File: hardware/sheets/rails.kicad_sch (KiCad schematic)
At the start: 55 parts, among them U1 LM5164DDA, U2 LM5164DDA, U3 LM51571-Q1, U4 DML3017LDC

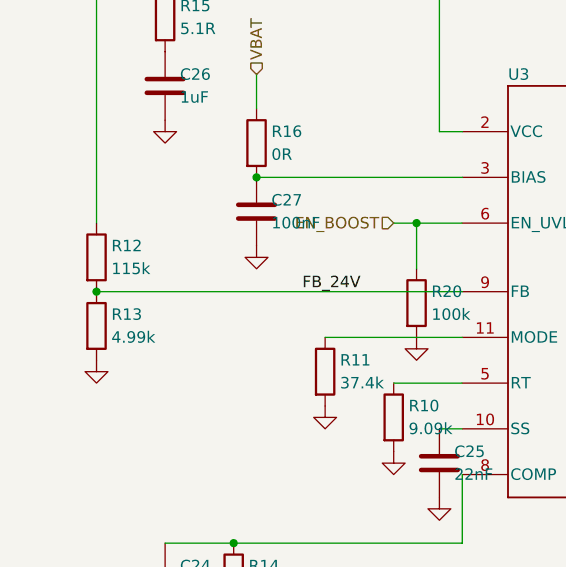
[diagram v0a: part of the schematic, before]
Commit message: hw(sch): Task 7 schematic review - three defects found and fixed
Every spec requirement traced to a sheet and refdes, read back from the
exported netlist rather than the drawing. 29 of 31 rows PASS; two carried
forward. Full write-up in hardware/docs/schematic-review.md.

F1 - Q1 carried the superseded SQJ415EP. That part was replaced by the
SQJ461EP on 2026-09-13 precisely because it is a 40 V device and the
SMBJ24A clamps at 38.9 V - 2.8% margin on the one part that sees every
vehicle transient. The replacement reached part-selection.md and the spec
but never the schematic, so a BOM built from it would have ordered the
wrong FET. Also closes the open gate-drive question: D1/R1 put Vgs at
-11 to -12.6 V, so the 16 mOhm column applies and the 0.78 W figure stands.

F2 - R2 and R3, the 0R links that short both windings of the common-mode
choke L2, were not marked DNP. A BOM would have stuffed the choke AND the
links; the links win and L2 becomes decorative. The board would work
perfectly and filter nothing, with no ERC or DRC check saying a word.
Both are now DNP, and gen_power_input.py learned to emit (dnp yes).

F3 - the 24 V feedback divider (115k/4.99k = 120k) conducts in deep sleep:
with the boost disabled, +24V still sits at ~12.35 V through L3 and D4, so
the divider drew 103 uA - larger than every other sleep contributor
combined, and absent from the spec 8.2 budget. Raised to 576k/24.9k, same
ratio, 20.5 uA. Revised budget ~94 uA typ / ~111 uA max against the 200 uA
target. C61 (10 pF, DNP) fitted as a Cff stuff option for the higher FB
impedance.

Carried forward: F4 (L1/L2 carry the full 7.0 A and have no thermal budget
- a 22 mOhm total DCR ceiling is now specified) and F5 (the spec's second
feed DNP footprints do not exist; needs a decision before Task 8 commits
to an outline).

Verification: ERC --severity-all --exit-code-violations exit=0, 0 errors,
0 warnings. 166 nets, unchanged by the fixes. DNP set read back from the
sheets: 31 parts. All six genera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
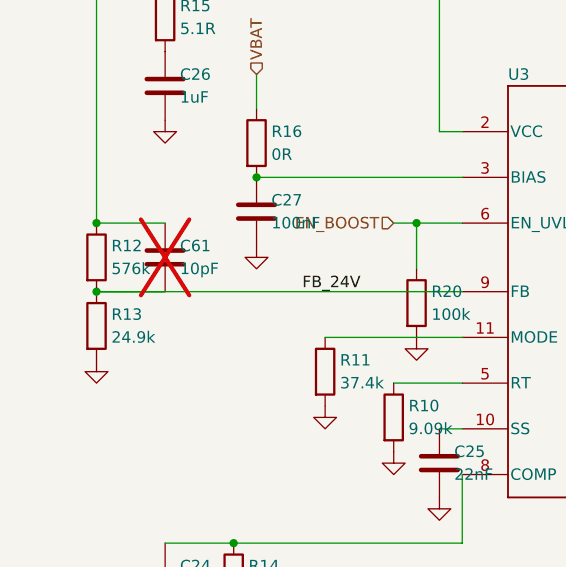
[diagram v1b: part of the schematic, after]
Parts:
- added C61: 10pF, symbol Device:C
- R12: value 115k -> 576k
- R13: value 4.99k -> 24.9k
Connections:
- net +24V: now also C61.1
- net FB_24V: now also C61.2
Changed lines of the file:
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@@
 	)
 	(junction
+		(at 30.48 134.62)
+		(diameter 0)
+		(color 0 0 0 0)
+	)
+	(junction
 		(at 76.2 45.72)
 		(diameter 0)
@@
 	(wire
 		(pts
+			(xy 38.1 142.24) (xy 30.48 142.24)
+		)
+		(stroke
+			(width 0)
+			(type default)
+		)
+	)
+	(wire
+		(pts
 			(xy 71.12 147.32) (xy 55.88 147.32)
 		)
@@
 	(wire
 		(pts
+			(xy 30.48 134.62) (xy 38.1 134.62)
+		)
+		(stroke
+			(width 0)
+			(type default)
+		)
+	)
+	(wire
+		(pts
 			(xy 116.84 195.58) (xy 116.84 190.5)
 		)
@@
 	)
 	(symbol
+		(lib_id "Device:C")
+		(at 38.1 138.43 0)
+		(unit 1)
+		(body_style 1)
+		(exclude_from_sim no)
+		(in_bom yes)
+		(on_board yes)
+		(in_pos_files yes)
+		(dnp yes)
+		(property "Reference" "C61"
+			(at 39.751 137.16 0)
+			(show_name no)
+			(do_not_autoplace no)
+			(effects
+				(font
+					(size 1.27 1.27)
+				)
+				(justify left)
+			)
+		)
+		(property "Value" "10pF"
+			(at 39.751 139.7 0)
+			(show_name no)
+			(do_not_autoplace no)
+			(effects
+				(font
+					(size 1.27 1.27)
+				)
+				(justify left)
+			)
+		)
+		(property "Footprint" ""
+			(at 38.1 138.43 0)
+			(hide yes)
+			(show_name no)
+			(do_not_autoplace no)
+			(effects
+				(font
+					(size 1.27 1.27)
+				)
+			)
+		)
+		(property "Datasheet" ""
+			(at 38.1 138.43 0)
+			(hide yes)
+			(show_name no)
+			(do_not_autoplace no)
+			(effects
+				(font
+					(size 1.27 1.27)
+				)
+			)
+		)
+		(property "Description" ""
+			(at 38.1 138.43 0)
+			(hide yes)
+			(show_name no)
+			(do_not_autoplace no)
+			(effects
+				(font
+					(size 1.27 1.27)
+				)
+			)
+		)
+		(pin "1"
+		)
+		(pin "2"
+		)
+		(instances
+			(project "mccan"
+				(path "/7410bb74-5653-4f1b-8c7c-ce17eb633f20/4a66277e-62b8-454b-8781-170494cf9f57"
+					(reference "C61")
+					(unit 1)
+				)
+			)
+		)
+	)
+	(symbol
 		(lib_id "Device:R")
 		(at 101.6 199.39 0)
@@
 			)
 		)
-		(property "Value" "4.99k"
+		(property "Value" "24.9k"
 			(at 32.131 147.32 0)
 			(show_name no)
@@
 			)
 		)
-		(property "Value" "115k"
+		(property "Value" "576k"
 			(at 32.131 139.7 0)
 			(show_name no)

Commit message: hw(sch): sweep every selected part into the schematic; D6+D7 become one PESD2CANFD24U-T
Closes the gap the Task 7 review's finding F1 was about: parts chosen in
prose had not reached the generators, which is exactly how the superseded
SQJ415EP survived five days in the schematic.

STRUCTURAL - the CAN ESD pair is now one part. D6 and D7 were two placeholder
"24V bidir" discretes; the Nexperia PESD2CANFD24U-T is a single SOT23 holding
both bidirectional elements (K1/K2/CC). New verified symbol in symlib.py built
from Table 2 of the datasheet, added to gen_mcu_can's lib_symbols, and
Device:D_TVS dropped from that sheet since D6/D7 were its only users.

The two protected pins land exactly on the CANH and CANL runs, so each run is
drawn as TWO segments meeting AT the pin rather than one segment the pin
happens to touch. A pin sitting mid-wire does connect, but this project has
already produced one silent connectivity defect of that shape (labels
mid-wire, 14 instances), so the pin is made a wire endpoint and junctioned.
Verified from the netlist rather than from ERC: D6.1 -> /CANH, D6.2 -> /CANL,
D6.3 -> GND.

Consolidating freed D7, so the diode series was renumbered to stay gapless:
the ignition-divider BAT54 D8 -> D7, the twelve RGB sense clamps D9-D20 ->
D8-D19, and the PROFET sense clamp D21 -> D20. Every designator series is
gapless: C1-61, D1-20, F1-5, J1-8, L1-6, Q1-9, R1-99, SW1-2, U1-9.

VALUE SWEEP - L4/L5 "22uH" -> XAL7070-223ME, L6 "51uH CM choke" ->
ACT45B-510-2P-TL003, C3 "220uF" -> "220uF 63V" (the SMBJ24A's 8/20 us clamp is
50.6 V, so a 50 V part has no margin), U7 -> PCA9685PW/Q900, the only
AEC-Q100 variant in the ordering table. U7's lib_id stays Driver_LED:PCA9685PW
- that is the stock symbol's name, and the package is the same TSSOP28. D4 was
already SS5PH102.

FOOTPRINT - installed the vendor SamacSys footprint and STEP model for the
Wurth choke as footprints/mccan.pretty/Wurth_WE-CMBNC_7448031002.kicad_mod and
3dmodels/. Its pads verify against t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
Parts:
- L4, L5: value 22uH -> XAL7070-223ME
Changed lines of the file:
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@@
 			)
 		)
-		(property "Value" "22uH"
+		(property "Value" "XAL7070-223ME"
 			(at 111.76 80.01 90)
 			(show_name no)
@@
 			)
 		)
-		(property "Value" "22uH"
+		(property "Value" "XAL7070-223ME"
 			(at 111.76 34.29 90)
 			(show_name no)

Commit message: hw(pcb): Task 8 step 0 - footprints assigned, 209 of 219 verified
Nothing in the project had a footprint except the PROFET's. Assignment now
lives in one auditable place, scripts/fpmap.py, which the four sheet
generators call when emitting each symbol's Footprint property. No generator
chooses a footprint of its own any more.

Three rules, and the reasoning is in the file rather than in a commit nobody
will read again: signal passives are 0603; a passive gets a bigger package
only for a stated reason; and nothing gets a footprint that has not been
checked to exist.

The reasons that drove a larger package:
- R2/R3, the 0R links bypassing the input choke windings, are 2512. They are
  DNP, but if anyone fits them for the tied-ground prototype they carry the
  entire 7.0 A night load, and a 0603 link is rated about 1 A.
- R52-R63, the RGB sense shunts, are 1206 for the FAULT case, not the normal
  7 mW. The package is sized on the understanding that firmware latches a
  shorted channel off; if that is ever dropped they must become 2512 1 W.
- The front-end ceramics are sized against the SMBJ24A's 8/20 us clamp of
  50.6 V, not the 38.9 V the distributor summaries quote. 100 nF fits 0805 at
  100 V; 1-2.2 uF at 63 V does not fit 0805; 10 uF at 63 V needs 1210.
- C20-C22 on +24 V are 1206 for DC-BIAS derating, a different reason - a 25 V
  X7R at 24 V keeps only 40-60% of nameplate.

Package identifications read from the datasheets rather than assumed:
NX5020UNBKS is SOT363/SC-88 (section 1), LM51571-Q1 RTE is WQFN-16 3x3 with a
1.66 mm exposed pad (so KiCad's EP1.675x1.675 is within tolerance), SS5PH102
is TO-277A, PESD2CANFD24U-T is SOT23.

FLAGGED, not silently accepted: the LM5164 DDA thermal pad is 3.4 x 2.8 mm on
the mechanical drawing and KiCad has no exact match. EP2.62x3.51 is the
closest by area (9.20 mm2 against 9.52) and is used for now, but that pad is
the part's heatsink on a thermally critical rail, so an exact DDA land pattern
should be drawn before fabr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
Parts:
- C10, C11, C14, C15, C16, C17, C23, C24, C25, C26, C27, C28, C29, C30, C31, C32, C33, C34, C61, C8, C9: footprint (none) -> Capacitor_SMD:C_0603_1608Metric
- C12, C20, C21, C22, C6: footprint (none) -> Capacitor_SMD:C_1206_3216Metric
- C13, C7: footprint (none) -> Capacitor_SMD:C_0805_2012Metric
- C18, C19: footprint (none) -> Capacitor_SMD:C_1210_3225Metric
- D4: footprint (none) -> Package_TO_SOT_SMD:TO-277A
- L3: footprint (none) -> Inductor_SMD:L_Coilcraft_XAL4030-XXX
- L4, L5: footprint (none) -> Inductor_SMD:L_Coilcraft_XAL7070-XXX
- R10, R11, R12, R13, R14, R15, R16, R17, R18, R19, R20, R21, R4, R5, R6, R7, R8, R9: footprint (none) -> Resistor_SMD:R_0603_1608Metric
- U1, U2: footprint (none) -> Package_SO:SOIC-8-1EP_3.9x4.9mm_P1.27mm_EP2.62x3.51mm
- U3: footprint (none) -> Package_DFN_QFN:QFN-16-1EP_3x3mm_P0.5mm_EP1.675x1.675mm
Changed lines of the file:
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@@
 			)
 		)
-		(property "Footprint" ""
+		(property "Footprint" "Capacitor_SMD:C_1206_3216Metric"
 			(at 48.26 67.31 0)
 			(hide yes)
@@
 			)
 		)
-		(property "Footprint" ""
+		(property "Footprint" "Capacitor_SMD:C_0603_1608Metric"
 			(at 38.1 138.43 0)
 			(hide yes)
@@
 			)
 		)
-		(property "Footprint" ""
+		(property "Footprint" "Resistor_SMD:R_0603_1608Metric"
 			(at 101.6 199.39 0)
 			(hide yes)
@@
 			)
 		)
-		(property "Footprint" ""
+		(property "Footprint" "Resistor_SMD:R_0603_1608Metric"
 			(at 38.1 111.76 0)
 			(hide yes)
@@
 			)
 		)
-		(property "Footprint" ""
+		(property "Footprint" "Resistor_SMD:R_0603_1608Metric"
 			(at 55.88 151.13 0)
 			(hide yes)
@@
 			)
 		)
-		(property "Footprint" ""
+		(property "Footprint" "Capacitor_SMD:C_1210_3225Metric"
 			(at 134.62 118.11 0)
 			(hide yes)
@@
 			)
 		)
-		(property "Footprint" ""
+		(property "Footprint" "Capacitor_SMD:C_1206_3216Metric"
 			(at 157.48 130.81 0)
 			(hide yes)
@@
 			)
 		)
-		(property "Footprint" ""
+		(property "Footprint" "Resistor_SMD:R_0603_1608Metric"
 			(at 30.48 146.05 0)
 			(hide yes)
@@
 			)
 		)
-		(property "Footprint" ""
+		(property "Footprint" "Capacitor_SMD:C_0603_1608Metric"
 			(at 96.52 72.39 0)
 			(hide yes)
@@
 			)
 		)
-		(property "Footprint" ""
+		(property "Footprint" "Capacitor_SMD:C_0603_1608Metric"
 			(at 68.58 161.29 0)
 			(hide yes)
@@
 			)
 		)
-		(property "Footprint" ""
+		(property "Footprint" "Capacitor_SMD:C_1206_3216Metric"
 			(at 149.86 130.81 0)
 			(hide yes)
@@
 			)
 		)
-		(property "Footprint" ""
+		(property "Footprint" "Capacitor_SMD:C_0805_2012Metric"
 			(at 40.64 67.31 0)
 			(hide yes)
@@
 			)
 		)
-		(property "Footprint" ""
+		(property "Footprint" "Resistor_SMD:R_0603_1608Metric"
 			(at 45.72 173.99 0)
 			(hide yes)
@@
 			)
 		)
-		(property "Footprint" ""
+		(property "Footprint" "Resistor_SMD:R_0603_1608Metric"
 			(at 63.5 156.21 0)
 			(hide yes)
@@
 			)
 		)
-		(property "Footprint" ""
+		(property "Footprint" "Resistor_SMD:R_0603_1608Metric"
 			(at 50.8 199.39 0)
 			(hide yes)
@@
 			)
 		)
-		(property "Footprint" ""
+		(property "Footprint" "Resistor_SMD:R_0603_1608Metric"
 			(at 58.42 41.91 0)
 			(hide yes)
@@
 			)
 		)
-		(property "Footprint" ""
+		(property "Footprint" "Capacitor_SMD:C_0603_1608Metric"
 			(at 132.08 34.29 0)
 			(hide yes)
@@
 			)
 		)
-		(property "Footprint" ""
+		(property "Footprint" "Capacitor_SMD:C_1210_3225Metric"
 			(at 142.24 118.11 0)
 			(hide yes)
@@
 			)
 		)
-		(property "Footprint" ""
+		(property "Footprint" "Resistor_SMD:R_0603_1608Metric"
 			(at 116.84 87.63 0)
 			(hide yes)
@@
 			)
 		)
-		(property "Footprint" ""
+		(property "Footprint" "Resistor_SMD:R_0603_1608Metric"
 			(at 248.92 46.99 0)
 			(hide yes)
@@
 			)
 		)
-		(property "Footprint" ""
+		(property "Footprint" "Capacitor_SMD:C_0805_2012Metric"
 			(at 50.8 29.21 0)
 			(hide yes)
@@
 			)
 		)
-		(property "Footprint" ""
+		(property "Footprint" "Resistor_SMD:R_0603_1608Metric"
 			(at 53.34 85.09 0)
 			(hide yes)
@@
 			)
 		)
-		(property "Footprint" ""
+		(property "Footprint" "Capacitor_SMD:C_0603_1608Metric"
 			(at 66.04 199.39 0)
 			(hide yes)
@@
 			)
 		)
-		(property "Footprint" ""
+		(property "Footprint" "Capacitor_SMD:C_0603_1608Metric"
 			(at 38.1 119.38 0)
 			(hide yes)
@@
 			)
 		)
-		(property "Footprint" ""
+		(property "Footprint" "Capacitor_SMD:C_0603_1608Metric"
 			(at 139.7 34.29 0)
 			(hide yes)
@@
 			)
 		)
-		(property "Footprint" ""
+		(property "Footprint" "Capacitor_SMD:C_1206_3216Metric"
 			(at 142.24 130.81 0)
 			(hide yes)
@@
 			)
 		)
-		(property "Footprint" ""
+		(property "Footprint" "Capacitor_SMD:C_0603_1608Metric"
 			(at 38.1 173.99 0)
 			(hide yes)
@@
 			)
 		)
-		(property "Footprint" ""
+		(property "Footprint" "Inductor_SMD:L_Coilcraft_XAL7070-XXX"
 			(at 107.95 76.2 0)
 			(hide yes)
@@
 			)
 		)
-		(property "Footprint" ""
+		(property "Footprint" "Package_SO:SOIC-8-1EP_3.9x4.9mm_P1.27mm_EP2.62x3.51mm"
 			(at 76.2 78.74 0)
 			(hide yes)
@@
 			)
 		)
-		(property "Footprint" ""
+		(property "Footprint" "Capacitor_SMD:C_0603_1608Metric"
 			(at 264.16 39.37 0)
 			(hide yes)
@@
 			)
 		)
-		(property "Footprint" ""
+		(property "Footprint" "Capacitor_SMD:C_0603_1608Metric"
 			(at 205.74 39.37 0)
 			(hide yes)
@@
 			)
 		)
-		(property "Footprint" ""
+		(property "Footprint" "Capacitor_SMD:C_0603_1608Metric"
 			(at 96.52 26.67 0)
 			(hide yes)
@@
 			)
 		)
-		(property "Footprint" ""
+		(property "Footprint" "Capacitor_SMD:C_0603_1608Metric"
 			(at 215.9 57.15 0)
 			(hide yes)
@@
 			)
 		)
-		(property "Footprint" ""
+		(property "Footprint" "Capacitor_SMD:C_0603_1608Metric"
 			(at 198.12 39.37 0)
 			(hide yes)
@@
 			)
 		)
-		(property "Footprint" ""
+		(property "Footprint" "Resistor_SMD:R_0603_1608Metric"
 			(at 116.84 41.91 0)
 			(hide yes)
@@
 			)
 		)
-		(property "Footprint" ""
+		(property "Footprint" "Capacitor_SMD:C_1206_3216Metric"
 			(at 43.18 29.21 0)
 			(hide yes)
@@
 			)
 		)
-		(property "Footprint" ""
+		(property "Footprint" "Resistor_SMD:R_0603_1608Metric"
 			(at 58.42 87.63 0)
 			(hide yes)
@@
 			)
 		)
-		(property "Footprint" ""
+		(property "Footprint" "Capacitor_SMD:C_0603_1608Metric"
 			(at 132.08 80.01 0)
 			(hide yes)
@@
 			)
 		)
-		(property "Footprint" ""
+		(property "Footprint" "Capacitor_SMD:C_0603_1608Metric"
 			(at 45.72 181.61 0)
 			(hide yes)
@@
 			)
 		)
-		(property "Footprint" ""
+		(property "Footprint" "Resistor_SMD:R_0603_1608Metric"
 			(at 48.26 125.73 0)
 			(hide yes)
@@
 			)
 		)
-		(property "Footprint" ""
+		(property "Footprint" "Capacitor_SMD:C_0603_1608Metric"
 			(at 50.8 207.01 0)
 			(hide yes)
@@
 			)
 		)
-		(property "Footprint" ""
+		(property "Footprint" "Resistor_SMD:R_0603_1608Metric"
 			(at 66.04 143.51 0)
 			(hide yes)
@@
 			)
 		)
-		(property "Footprint" ""
+		(property "Footprint" "Inductor_SMD:L_Coilcraft_XAL7070-XXX"
 			(at 107.95 30.48 0)
 			(hide yes)
@@
 			)
 		)
-		(property "Footprint" ""
+		(property "Footprint" "Capacitor_SMD:C_0603_1608Metric"
 			(at 256.54 39.37 0)
 			(hide yes)
@@
 			)
 		)
-		(property "Footprint" ""
+		(property "Footprint" "Capacitor_SMD:C_0603_1608Metric"
 			(at 101.6 207.01 0)
 			(hide yes)
@@
 			)
 		)
-		(property "Footprint" ""
+		(property "Footprint" "Package_DFN_QFN:QFN-16-1EP_3x3mm_P0.5mm_EP1.675x1.675mm"
 			(at 96.52 142.24 0)
 			(hide yes)
@@
 			)
 		)
-		(property "Footprint" ""
+		(property "Footprint" "Package_SO:SOIC-8-1EP_3.9x4.9mm_P1.27mm_EP2.62x3.51mm"
 			(at 76.2 33.02 0)
 			(hide yes)
@@
 			)
 		)
-		(property "Footprint" ""
+		(property "Footprint" "Resistor_SMD:R_0603_1608Metric"
 			(at 116.84 34.29 0)
 			(hide yes)
@@
 			)
 		)
-		(property "Footprint" ""
+		(property "Footprint" "Inductor_SMD:L_Coilcraft_XAL4030-XXX"
 			(at 127 118.11 0)
 			(hide yes)
@@
 			)
 		)
-		(property "Footprint" ""
+		(property "Footprint" "Resistor_SMD:R_0603_1608Metric"
 			(at 116.84 80.01 0)
 			(hide yes)
@@
 			)
 		)
-		(property "Footprint" ""
+		(property "Footprint" "Capacitor_SMD:C_0603_1608Metric"
 			(at 139.7 80.01 0)
 			(hide yes)
@@
 			)
 		)
-		(property "Footprint" ""
+		(property "Footprint" "Resistor_SMD:R_0603_1608Metric"
 			(at 30.48 138.43 0)
 			(hide yes)
@@
 			)
 		)
-		(property "Footprint" ""
+		(property "Footprint" "Capacitor_SMD:C_0603_1608Metric"
 			(at 48.26 133.35 0)
 			(hide yes)
@@
 			)
 		)
-		(property "Footprint" ""
+		(property "Footprint" "Capacitor_SMD:C_0603_1608Metric"
 			(at 116.84 199.39 0)
 			(hide yes)
@@
 			)
 		)
-		(property "Footprint" ""
+		(property "Footprint" "Package_TO_SOT_SMD:TO-277A"
 			(at 134.62 127 0)
 			(hide yes)

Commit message: hw(pcb): resolve D4 and U4, give GND_IN its own island, stop leaving stubs
Four things that had all been blocking a clean board, plus the pass of routing
they unblocked.

D4 is a TO-277A, whose third pad is the cathode tab.  Device:D_Schottky has no
pin 3, so schematic parity reported the tab as a net with no corresponding pin
however the pad was aliased -- aliasing pads is not a fix for a symbol that is
missing a pin.  mccan_parts:D_SCHOTTKY_TAB is that symbol with a hidden pin 3
stacked on the cathode, which is what the part actually is.

U4 was BLOCKED since Task 8 step 0 on an apparent pin-1 disagreement between two
figures of DS46371.  There is no disagreement: the Suggested Pad Layout is a bare
land pattern with no pin names, drawn in a different orientation from the Package
Outline, and the three figures that do carry pin names all agree.  Pin 1 top-left
in top view, counter-clockwise; pad 13 is the exposed pad and it is VIN, not GND.
The reasoning is written out in fpmap.py so it is not re-litigated.  fpmap's
unassignable list is now empty and says why it should stay that way.

GND_IN gets its own F.Cu island rather than sharing the pour.  GND and GND_IN are
separate nets that meet at exactly two places, L2 winding B and R3; nothing in DRC
enforces that, because a pour never shorts to a foreign net, so check_grounds.py
is the guard and it now passes: all 12 GND_IN pads inside the island, no GND pads
in it.

_ar_prune was deleting whole tracks when it should have been trimming them, and
was doing its reachability walk without regard for which layer a piece was on.
It is now layer-aware and junction-based, and trims rather than deletes.  That
takes the board from 9 dangling vias and 1 dangling track to none of either.

Also: SolderWire footprints are BOM-excluded in the library and the symbols
disagreed, which parity reported seven times over -- the footprints are right, so
in_bom() now follows them.  Silk references that collided move to F.Fab instead
of bein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
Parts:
- D4: symbol Device:D_Schottky -> mccan_parts:D_SCHOTTKY_TAB
- U4: footprint (none) -> Package_DFN_QFN:DFN-12-1EP_3x3mm_P0.5mm_EP2.05x2.86mm
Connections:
- net +24V: now also D4.3 (K)
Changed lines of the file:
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@@
 			)
 		)
-		(property "Footprint" ""
+		(property "Footprint" "Package_DFN_QFN:DFN-12-1EP_3x3mm_P0.5mm_EP2.05x2.86mm"
 			(at 228.6 45.72 0)
 			(hide yes)
@@
 	)
 	(symbol
-		(lib_id "Device:D_Schottky")
+		(lib_id "mccan_parts:D_SCHOTTKY_TAB")
 		(at 134.62 127 180)
 		(unit 1)
@@
 		(pin "2"
 		)
-		(instances
+		(pin "3"
+		)
+		(instances

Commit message: hw(rails): delete the 24 V boost and the switched 3V3 domain
Co-Authored-By: Claude Sonnet 5.5 <noreply@anthropic.com>
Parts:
- removed C18, C19: 10uF, Capacitor_SMD:C_1210_3225Metric, symbol Device:C
- removed C20, C21, C22: 4.7uF, Capacitor_SMD:C_1206_3216Metric, symbol Device:C
- removed C23: 10nF, Capacitor_SMD:C_0603_1608Metric, symbol Device:C
- removed C24: 100pF, Capacitor_SMD:C_0603_1608Metric, symbol Device:C
- removed C25: 22nF, Capacitor_SMD:C_0603_1608Metric, symbol Device:C
- removed C26, C30, C31: 1uF, Capacitor_SMD:C_0603_1608Metric, symbol Device:C
- removed C27, C33: 100nF, Capacitor_SMD:C_0603_1608Metric, symbol Device:C
- removed C32: 1nF, Capacitor_SMD:C_0603_1608Metric, symbol Device:C
- removed C34: 10uF, Capacitor_SMD:C_0603_1608Metric, symbol Device:C
- removed C61: 10pF, Capacitor_SMD:C_0603_1608Metric, symbol Device:C
- removed D4: SS5PH102, Package_TO_SOT_SMD:TO-277A, symbol mccan_parts:D_SCHOTTKY_TAB
- removed L3: 6.8uH XAL4030-682ME, Inductor_SMD:L_Coilcraft_XAL4030-XXX, symbol Device:L
- removed R10: 9.09k, Resistor_SMD:R_0603_1608Metric, symbol Device:R
- removed R11: 37.4k, Resistor_SMD:R_0603_1608Metric, symbol Device:R
- removed R12: 576k, Resistor_SMD:R_0603_1608Metric, symbol Device:R
- removed R13: 24.9k, Resistor_SMD:R_0603_1608Metric, symbol Device:R
- removed R14: 2.61k, Resistor_SMD:R_0603_1608Metric, symbol Device:R
- removed R15: 5.1R, Resistor_SMD:R_0603_1608Metric, symbol Device:R
- removed R16: 0R, Resistor_SMD:R_0603_1608Metric, symbol Device:R
- removed R20: 100k, Resistor_SMD:R_0603_1608Metric, symbol Device:R
- removed R21: 100R, Resistor_SMD:R_0603_1608Metric, symbol Device:R
- removed U3: LM51571-Q1, Package_DFN_QFN:QFN-16-1EP_3x3mm_P0.5mm_EP1.675x1.675mm, symbol mccan_parts:LM51571QRTERQ1
- removed U4: DML3017LDC, Package_DFN_QFN:DFN-12-1EP_3x3mm_P0.5mm_EP2.05x2.86mm, symbol mccan_parts:DML3017LDC
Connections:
- net EN_3V3SW renamed EN_5V
- no-connect marks 4 -> 2
